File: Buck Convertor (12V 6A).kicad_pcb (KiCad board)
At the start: 4 copper layers, 74.6 x 39.6 mm, 45 parts, among them J1 1726480102, J2 1726480102, J3 Conn_01x03, J4 Conn_01x03, Q1 2N7002, Q2 NTD2955T4G, U1 SIC438BED-T1-GE3

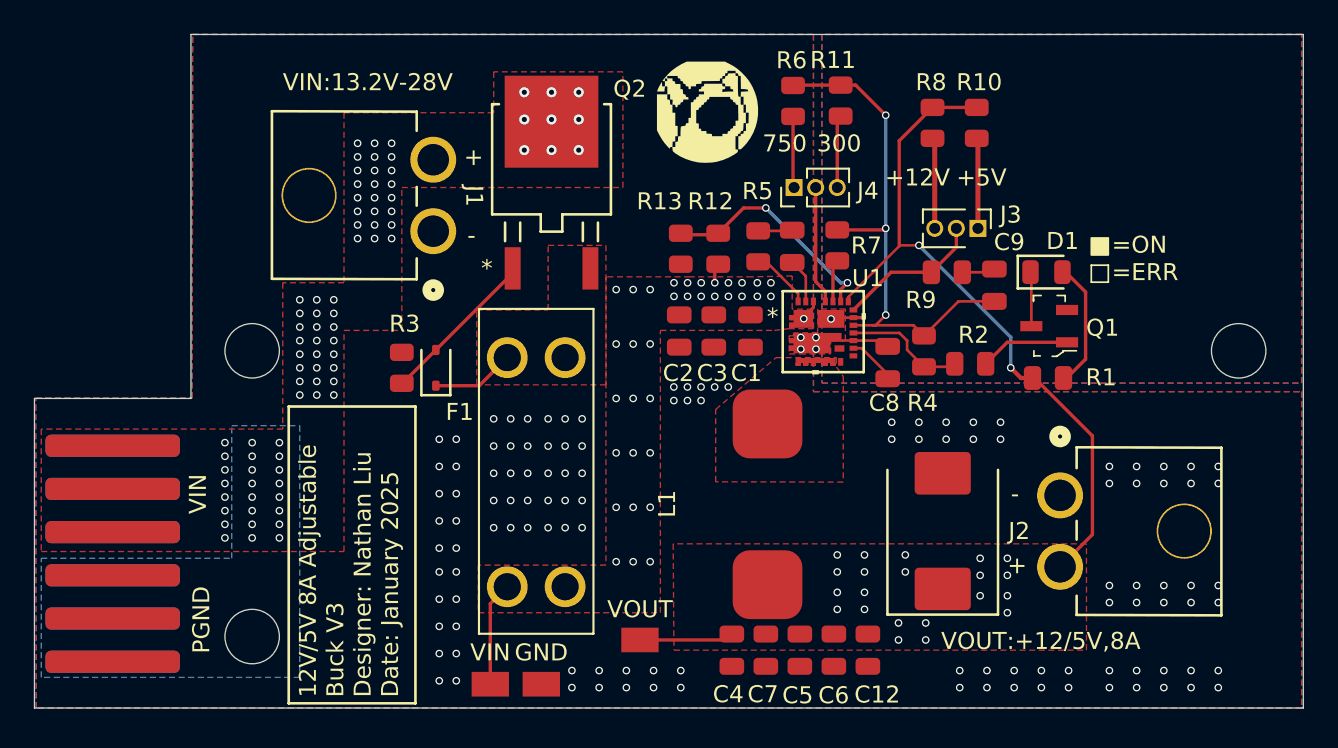
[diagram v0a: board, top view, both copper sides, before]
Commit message: Fixed PFET being wrong size
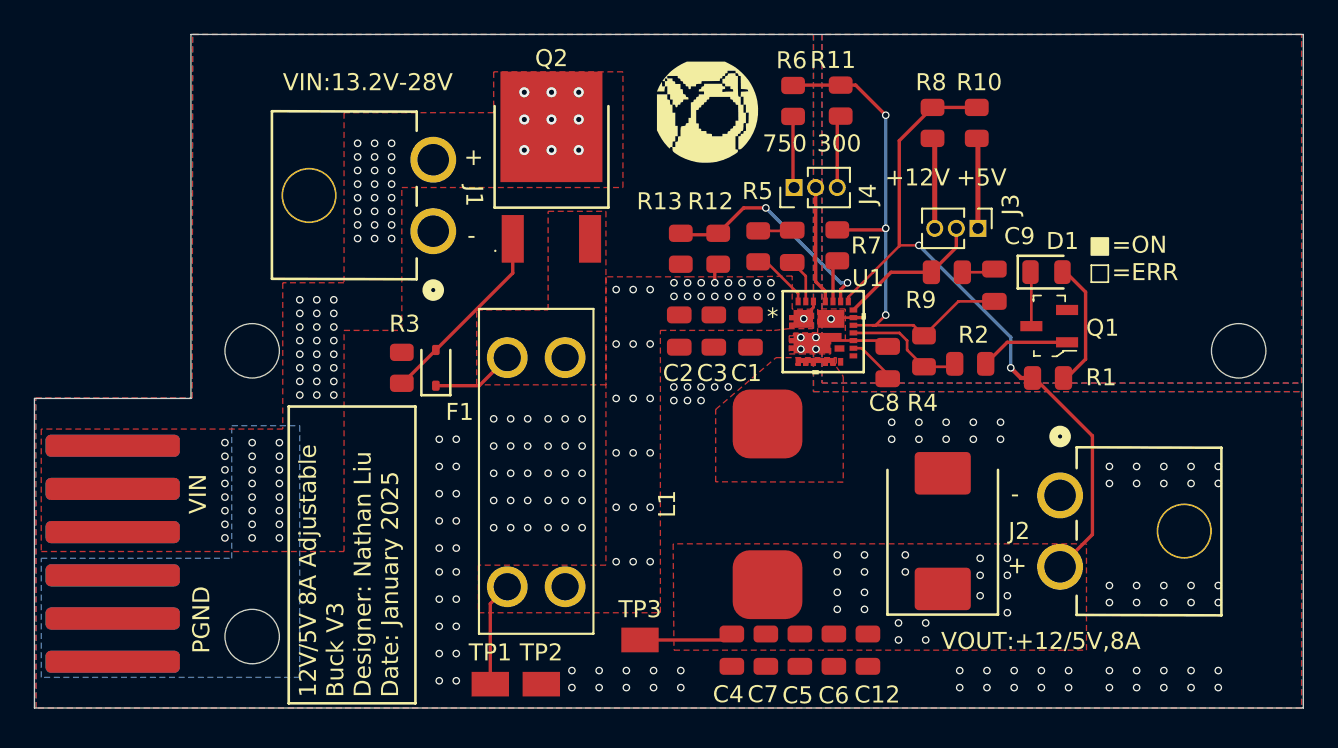
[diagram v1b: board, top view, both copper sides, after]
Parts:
- J3, J4: footprint Buck12V6A:PinHeader_1x03_P1.27mm_Vertical -> Connector_PinHeader_1.27mm:PinHeader_1x03_P1.27mm_Vertical
- Q2: footprint Buck12V6A:DPAK-369C_ONS -> Buck12V6A:TO-252-2_L6.6-W6.1-P4.57-LS9.9-TL-CW
- moved Q2 1.39 mm to (125.6, 104.7), turned to 90 degrees
- renumbered VIN to TP1, GND to TP2, VOUT to TP3
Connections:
- Q2 pad 1: /VINRAW -> Net-(Q2-G)
- Q2 pad 2: Net-(Q2-G) -> /VINRAW
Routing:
- net Net-(Q2-G): track 9.48 -> 11.2 mm
